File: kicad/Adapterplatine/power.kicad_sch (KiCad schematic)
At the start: 4 parts, among them X1 Conn_01x02_Pin, X3 Conn_01x02_Pin

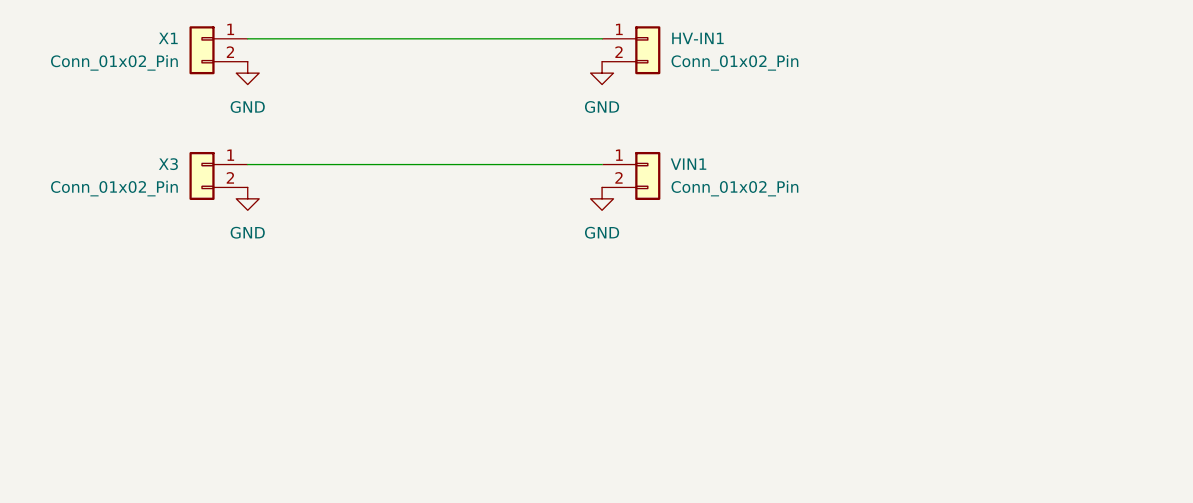
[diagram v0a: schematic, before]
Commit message: Abschlussbericht angefangen/ Adapterplatine ECR DCR
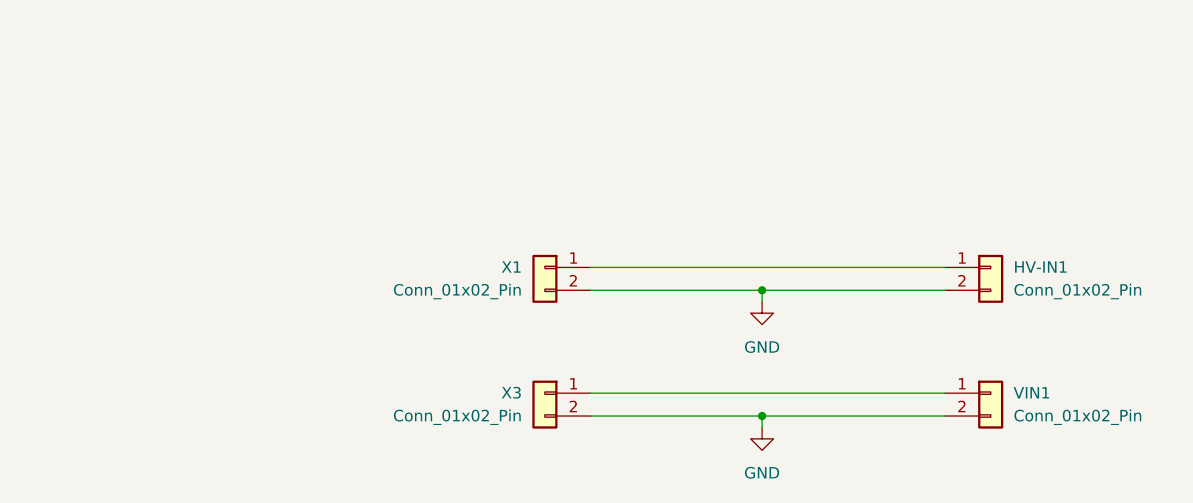
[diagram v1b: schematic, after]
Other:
- moved on the sheet: HV-IN1, VIN1, X1, X3

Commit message: Adapterplatine Version 1.0 final
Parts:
- HV-IN1, VIN1: footprint Connector_Phoenix_MSTB:PhoenixContact_MSTBA_2,5_2-G_1x02_P5.00mm_Horizontal -> Connector_Phoenix_MSTB:PhoenixContact_MSTBVA_2,5_2-G_1x02_P5.00mm_Vertical
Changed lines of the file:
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@@
 			)
 		)
-		(property "Footprint" "Connector_Phoenix_MSTB:PhoenixContact_MSTBA_2,5_2-G_1x02_P5.00mm_Horizontal"
+		(property "Footprint" "Connector_Phoenix_MSTB:PhoenixContact_MSTBVA_2,5_2-G_1x02_P5.00mm_Vertical"
 			(at 167.64 90.17 0)
 			(hide yes)
@@
 		)
 		(property "Description" "Generic connector, single row, 01x02, script generated (kicad-library-utils/schlib/autogen/connector/)"
+			(at 167.64 90.17 0)
+			(hide yes)
+			(show_name no)
+			(do_not_autoplace no)
+			(effects
+				(font
+					(size 1.27 1.27)
+				)
+			)
+		)
+		(property "Hersteller" ""
+			(at 167.64 90.17 0)
+			(hide yes)
+			(show_name no)
+			(do_not_autoplace no)
+			(effects
+				(font
+					(size 1.27 1.27)
+				)
+			)
+		)
+		(property "Herstellerbezeichnung" ""
+			(at 167.64 90.17 0)
+			(hide yes)
+			(show_name no)
+			(do_not_autoplace no)
+			(effects
+				(font
+					(size 1.27 1.27)
+				)
+			)
+		)
+		(property "Alternative" ""
 			(at 167.64 90.17 0)
 			(hide yes)
@@
 			)
 		)
-		(property "Footprint" "Connector_Phoenix_MSTB:PhoenixContact_MSTBA_2,5_2-G_1x02_P5.00mm_Horizontal"
+		(property "Footprint" "Connector_Phoenix_MSTB:PhoenixContact_MSTBVA_2,5_2-G_1x02_P5.00mm_Vertical"
 			(at 167.64 104.14 0)
 			(hide yes)
@@
 			(at 167.64 104.14 0)
 			(hide yes)
+			(show_name no)
+			(do_not_autoplace no)
+			(effects
+				(font
+					(size 1.27 1.27)
+				)
+			)
+		)
+		(property "Hersteller" ""
+			(at 167.64 104.14 0)
+			(hide yes)
+			(show_name no)
+			(do_not_autoplace no)
+			(effects
+				(font
+					(size 1.27 1.27)
+				)
+			)
+		)
+		(property "Herstellerbezeichnung" ""
+			(at 167.64 104.14 0)
+			(hide yes)
+			(show_name no)
+			(do_not_autoplace no)
+			(effects
+				(font
+					(size 1.27 1.27)
+				)
+			)
+		)
+		(property "Alternative" ""
+			(at 167.64 104.14 0)
+			(hide yes)
